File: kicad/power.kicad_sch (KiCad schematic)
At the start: 97 parts, among them J1 USB_C_Receptacle_USB2.0_16P, J11 Balance, J3 XT30UPB-M, Q1 AO4407A, Q2 80N03F, Q3 80N03F, SW1 Power, U13 BQ7791501, U4 AP64500SP-13, U5 CH224A, U7 BQ25798, U8 HT7550-1, U9 XC6206P332MR

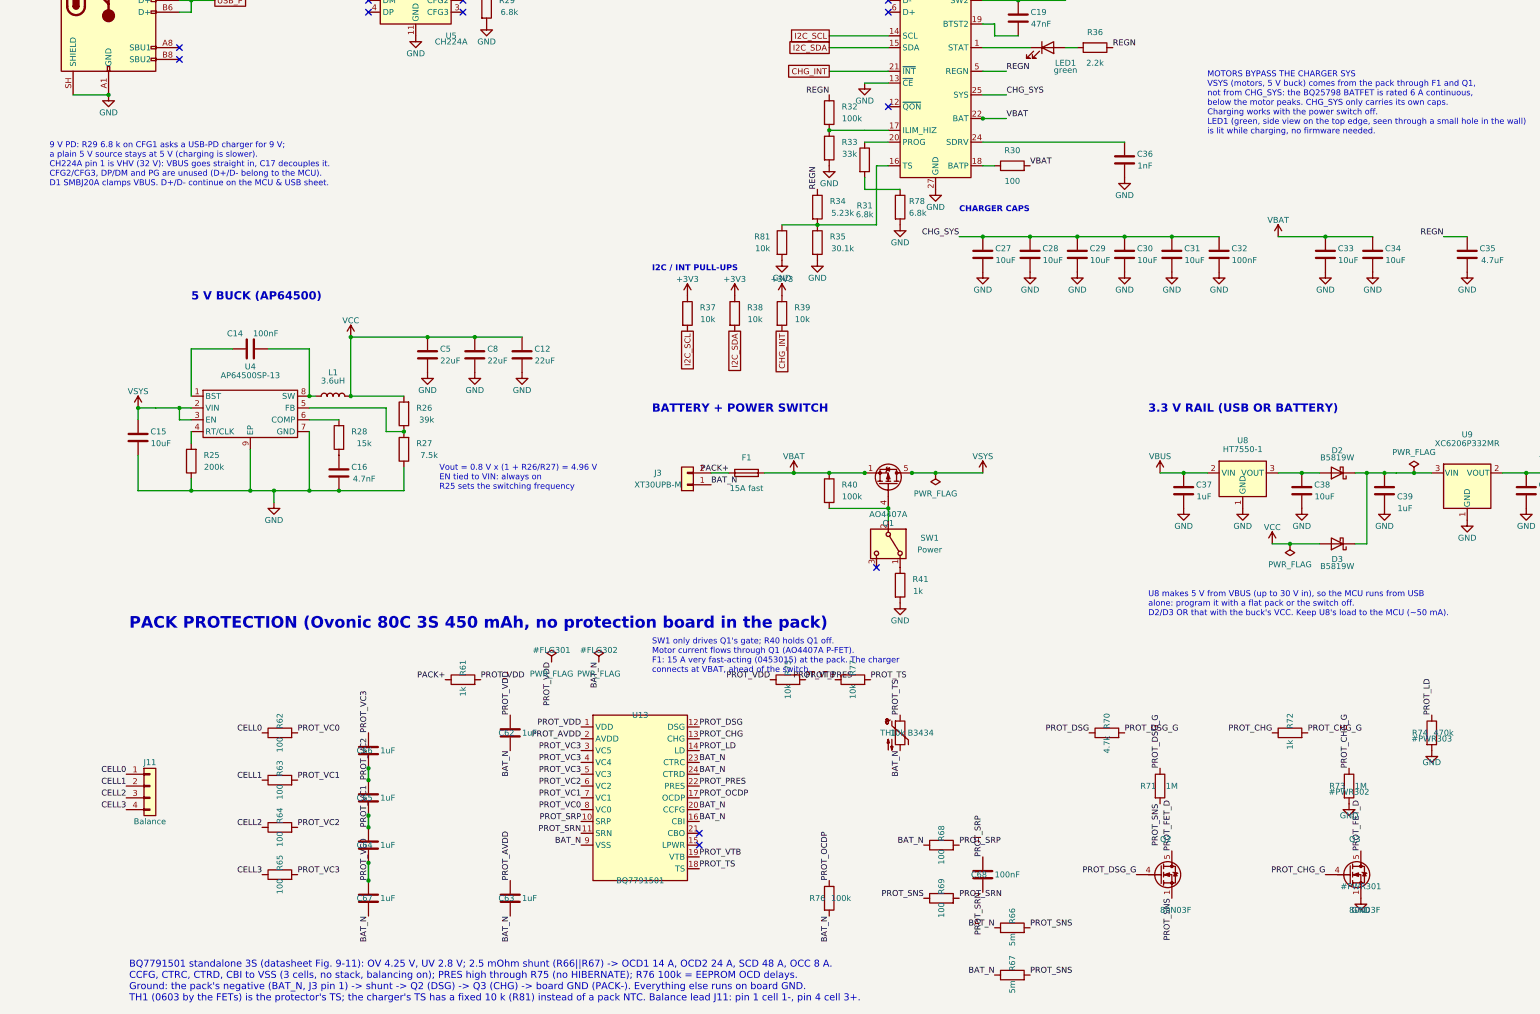
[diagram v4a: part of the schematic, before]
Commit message: Fix the buck inductor, soft-start VSYS and limit motor current
Circuit (goosebrain.py, PARTS.md, schematic):
- L1 is a Coilcraft XAL5030-222 (Isat 9.2 A, the AP64500's max current
  limit). The old CR4030 saturated at about 3.1 A.
- VSYS soft start and clamp: C71 gate-drain and C72 gate-source on Q1,
  R40 27k, R41 10k, and an SMF14A TVS (D4) on VSYS.
- Each DRV8848 chops at about 1.33 A per bridge: 0.15 R sense resistors
  on AISEN/BISEN and a 15k/10k VREF divider from VINT, so six stalled
  motors can't reach the protector's OCD1 trip.
- U4 gets a second 10 uF (C73) and a 100 nF (C74) at VIN.
- Stock swaps after a full JLC stock check: D4 to the Littelfuse SMF14A,
  the sense resistors to YAGEO RL1206FR-7W0R15L (500 mW).

Board:
- New parts placed and routed. The sense resistors are close to their
  pins; U2's B-side runs on F.Cu only.
- 22 more VSYS vias (Q1 drain to the In3 plane, each driver's VM caps,
  both ends of U4's VIN jumper).
- C63 (AVDD) and C68 (SRP-SRN) moved next to the BQ7791501.
- Goose logo on the back silkscreen.
- Review 63: DRC 0 errors, unrouted 0, parity clean, no new DRC types.

tools/fab.py adds per-package rotation offsets read off JLC's placement
preview. The README covers them, the D4 polarity check, the corrected
current limits and the low-stock parts.

Co-Authored-By: Claude Opus 5.5 <noreply@anthropic.com>
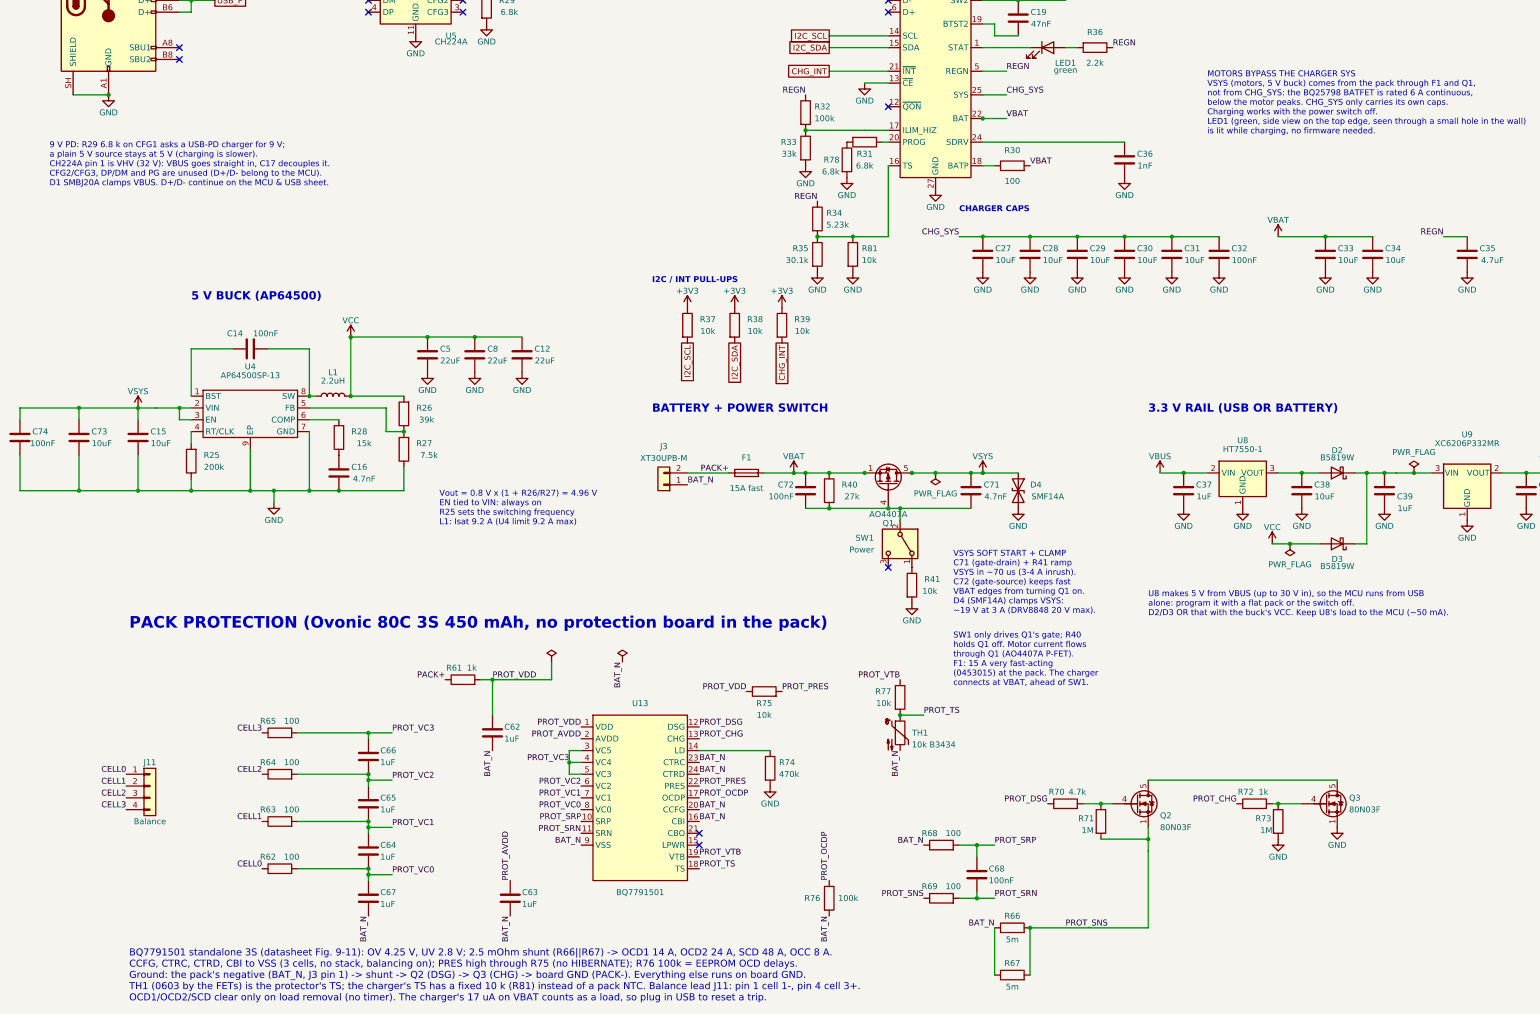
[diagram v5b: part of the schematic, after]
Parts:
- added C71: 4.7nF, Capacitor_SMD:C_0402_1005Metric, symbol Device:C
- added C72: 100nF, Capacitor_SMD:C_0805_2012Metric, symbol Device:C
- added C73: 10uF, Capacitor_SMD:C_0805_2012Metric, symbol Device:C
- added C74: 100nF, Capacitor_SMD:C_0402_1005Metric, symbol Device:C
- added D4: SMF14A, Diode_SMD:D_SMF, symbol Device:D_TVS
- L1: value 3.6uH -> 2.2uH; footprint Inductor_SMD_Wurth:L_Wurth_WE-LQSH-4020 -> hexy:L_Coilcraft_XAL5030; LCSC Part # C7588667 -> C920280; MPN CR4030-3R6M -> XAL5030-222MEC; Manufacturer Ceaiya -> Coilcraft
- R40: value 100k -> 27k; LCSC Part # C25741 -> C25771; MPN 0402WGF1003TCE -> 0402WGF2702TCE
- R41: value 1k -> 10k; LCSC Part # C11702 -> C25744; MPN 0402WGF1001TCE -> 0402WGF1002TCE
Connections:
- net GND: now also C73.1, C74.1, D4.2 (A2)
- net VBAT: now also C72.1
- net VSYS: now also C71.2, C73.2, C74.2, D4.1 (A1)
- net at Q1.4 (G), R40.2, SW1.2 (B): now also C71.1, C72.2
- net PROT_CHG_G: no longer names the net of Q3.4 (G), R72.2, R73.1
- net PROT_DSG_G: no longer names the net of Q2.4 (G), R70.2, R71.1
- net PROT_FET_D: no longer names the net of Q2.5 (D), Q3.5 (D)
- net PROT_LD: no longer names the net of R74.1, U13.14 (LD)
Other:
- note added: "SW1 only drives Q1's gate; R40 holds Q1 off. Motor current flows through Q1 (AO4407A P-FET). F1: 15 A very fast-acting (0453015) at the pack. The charger connects at VBAT, ahead of SW1."
- note added: "VSYS SOFT START + CLAMP C71 (gate-drain) + R41 ramp VSYS in ~70 us (3-4 A inrush). C72 (gate-source) keeps fast VBAT edges from turning Q1 on. D4 (SMF14A) clamps VSYS: ~19 V at 3 A (DRV8848 20 V max)."
- note added: "Vout = 0.8 V x (1 + R26/R27) = 4.96 V EN tied to VIN: always on R25 sets the switching frequency L1: Isat 9.2 A (U4 limit 9.2 A max)"
- note removed: "SW1 only drives Q1's gate; R40 holds Q1 off. Motor current flows through Q1 (AO4407A P-FET). F1: 15 A very fast-acting (0453015) at the pack. The charger connects at VBAT, ahead of the switch."
- note removed: "Vout = 0.8 V x (1 + R26/R27) = 4.96 V EN tied to VIN: always on R25 sets the switching frequency"
- moved on the sheet: C62, C64, C65, C66, C68, J3, Q2, Q3, R32, R33, R34, R35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
